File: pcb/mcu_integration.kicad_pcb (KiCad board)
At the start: 4 copper layers, 90.2 x 95.9 mm, 103 parts, among them IC1 TL7660IDGKR, IC10 AD844_OPAMP_MEL, IC3 FOD814_OPTO_NOSHD, IC5 FOD814_OPTO_MEL, IC6 AD844_OPAMP_AL, IC7 FOD814_OPTO_AL, IC8 AD844_OPAMP_NOSHD, IC9 TL081IDT, J5 DM3BT-DSF-PEJS, M1 MountingHole_Pad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

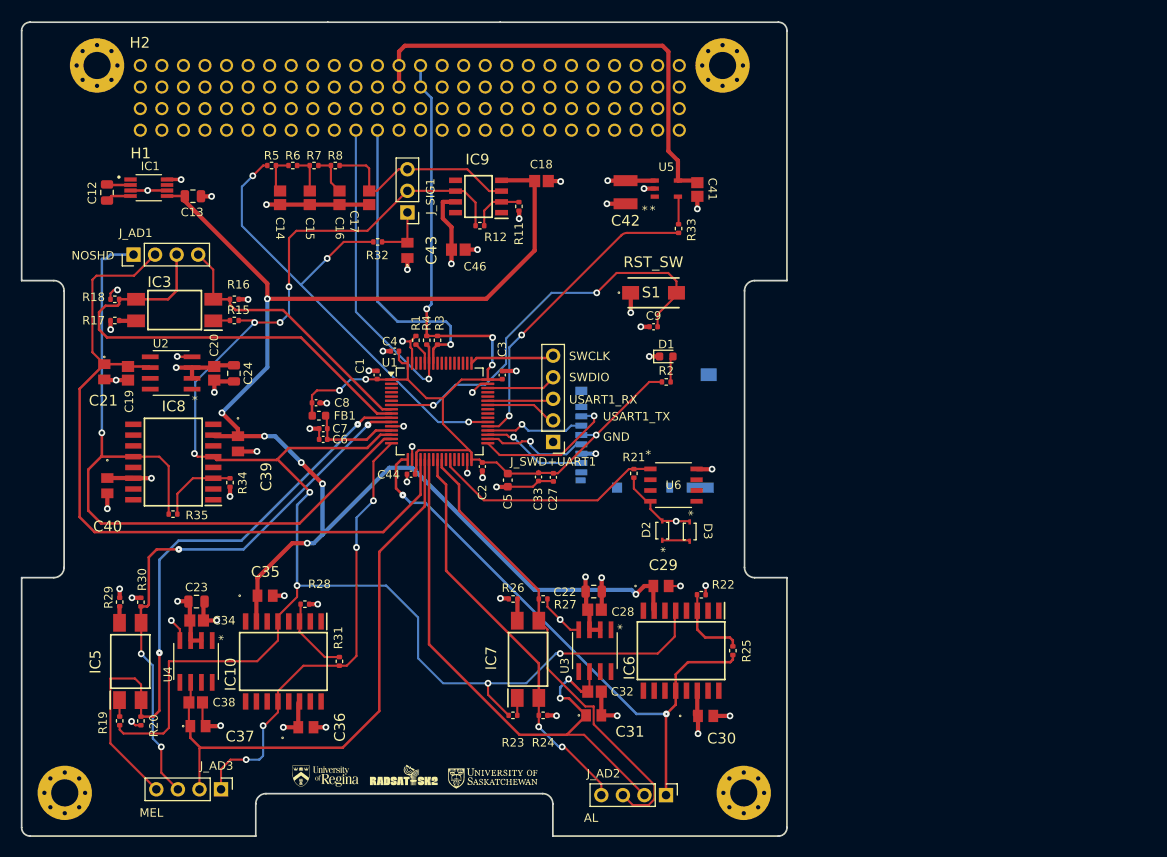
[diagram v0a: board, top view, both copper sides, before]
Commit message: Added copper pours to top and bottom layer, added 3.3v plane, spaced ICs to fit melanin caps, ungrounded connection pads, added stitching vias to outer edge
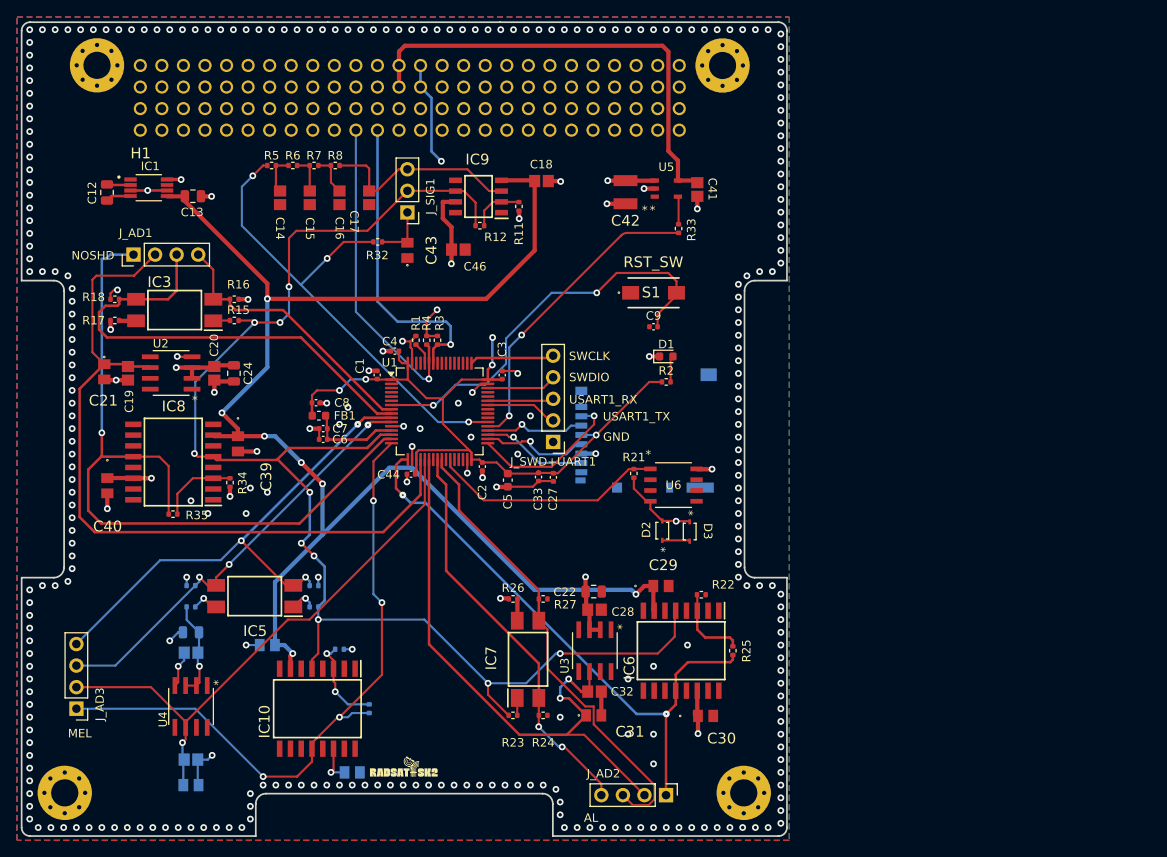
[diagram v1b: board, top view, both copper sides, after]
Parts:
- C23, C34, C35, C36, C37, C38, R19, R20, R28, R29, R30, R31: moved to B.Cu
- moved R19 26.5 mm to (127.0, 120.5), turned to 0 degrees
- moved R20 25.9 mm to (127.0, 118.0), turned to 0 degrees
- moved J_AD3 19.5 mm to (99.0, 132.5), turned to 180 degrees
- moved IC5 16.6 mm to (120.0, 119.2), turned to 180 degrees
- moved R29 8.42 mm to (112.5, 120.5), turned to 180 degrees
- moved C36 7.62 mm to (131.5, 140.0)
- moved C37 7.00 mm to (112.5, 141.5)
- moved IC10 6.86 mm to (127.4, 132.5)
- moved C38 6.76 mm to (112.5, 138.5)
- moved R28 6.70 mm to (130.0, 125.5)
- moved R31 6.59 mm to (133.5, 132.5)
- moved R30 6.21 mm to (112.5, 118.0), turned to 0 degrees
- moved C35 5.82 mm to (121.5, 125.0), turned to 180 degrees
- moved U4 5.34 mm to (112.5, 132.2)
- moved C34 3.84 mm to (112.5, 125.9), turned to 180 degrees
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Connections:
- M1 pad 1: GND -> unconnected-(M1-Pad1)
- M2 pad 1: GND -> unconnected-(M2-Pad1)
- M3 pad 1: GND -> unconnected-(M3-Pad1)
- M4 pad 1: GND -> unconnected-(M4-Pad1)
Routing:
- net GND: track 129.4 -> 90.8 mm, vias 51 -> 314
- net ADC1_IN0_SINE: track 201.3 -> 169.8 mm, vias 8 -> 10
- net ADC1_IN2_OPAMP_MEL: track 54.2 -> 77.8 mm
- net 3.3V Output: track 124.9 -> 101.8 mm, vias 6 -> 7
- net ADC1_IN12_OPTO_F_MEL: track 77.5 -> 59.5 mm, vias 2 -> 3
- net ADC1_IN13_OPTO_E_MEL: track 65.2 -> 50.7 mm, vias 4 -> 3
- net -5V Output: track 171.4 -> 176.2 mm
- net +5V: track 62.8 -> 65.2 mm, vias 13 -> 12
- net ADC1_IN5_VREF_MEL: track 68.0 -> 66.4 mm, vias 0 -> 1
- net Net-(IC10--IN): track 9.23 -> 10.7 mm, vias 0 -> 2
- net Net-(IC5-C): track 1.95 -> 3.29 mm, vias 0 -> 1
- net /SPI2_CS_NSS: track 16.9 -> 18.3 mm
- net Net-(IC5-AK): track 1.95 -> 3.06 mm, vias 0 -> 1
- added copper zone on In1.Cu, net 3.3V Output
- added copper zone on B.Cu, net GND
- added copper zone on F.Cu, net GND

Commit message: Conformed to JLC DFM
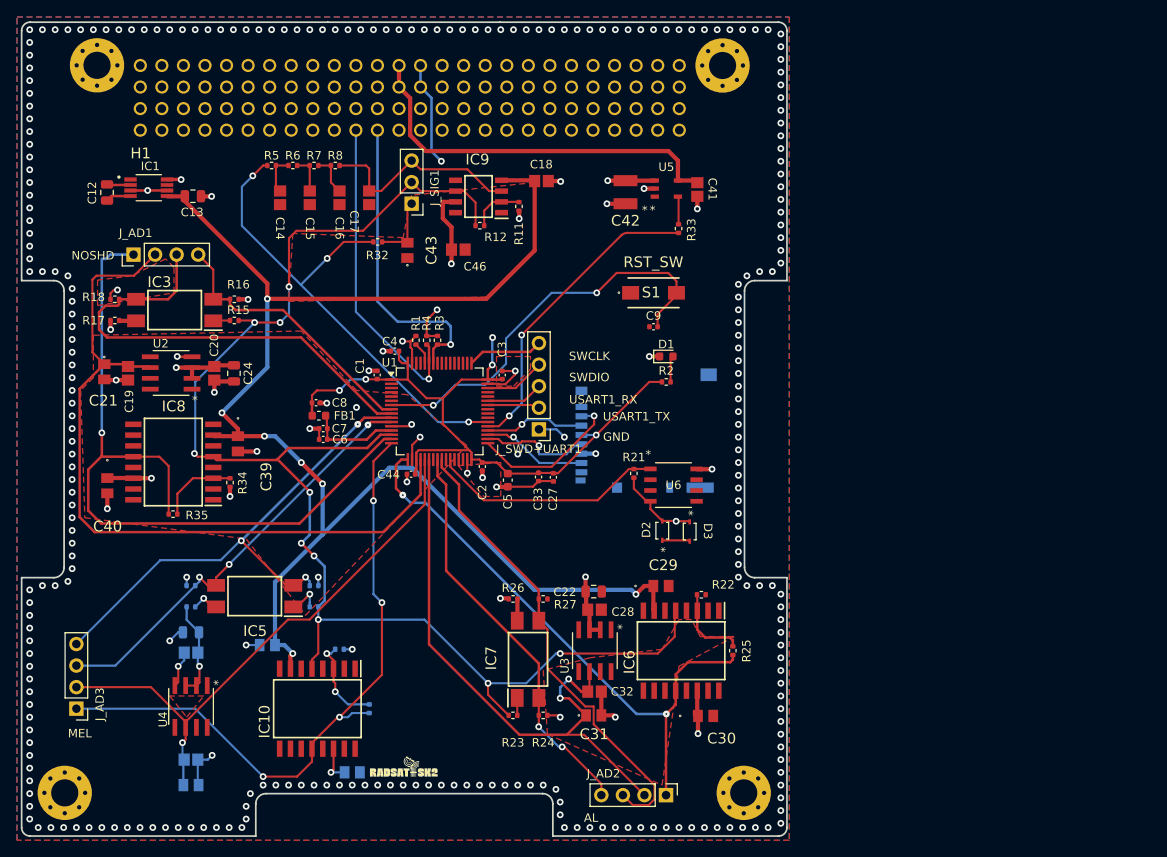
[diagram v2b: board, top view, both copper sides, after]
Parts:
- moved J_SWD+UART1 2.24 mm to (153.5, 99.6)
- moved J_SIG1 1.14 mm to (138.5, 73.0)
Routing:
- net GND: track 90.8 -> 101.4 mm, vias 314 -> 299
- net +5V_EXT: track 54.6 -> 46.3 mm
- net /USART1_TX: track 8.39 -> 6.16 mm
- net Net-(J_SIG1-Pin_1): track 6.61 -> 7.84 mm
- net Net-(IC5-AK): track 3.06 -> 4.07 mm
- net ADC1_IN0_SINE: track 169.8 -> 170.7 mm
- net RC_OUTPUT: track 24.0 -> 24.9 mm
- net /USART1_RX: track 7.55 -> 6.74 mm
- net /SWCLK: track 9.71 -> 8.93 mm
- net /SWDIO: track 7.94 -> 7.17 mm

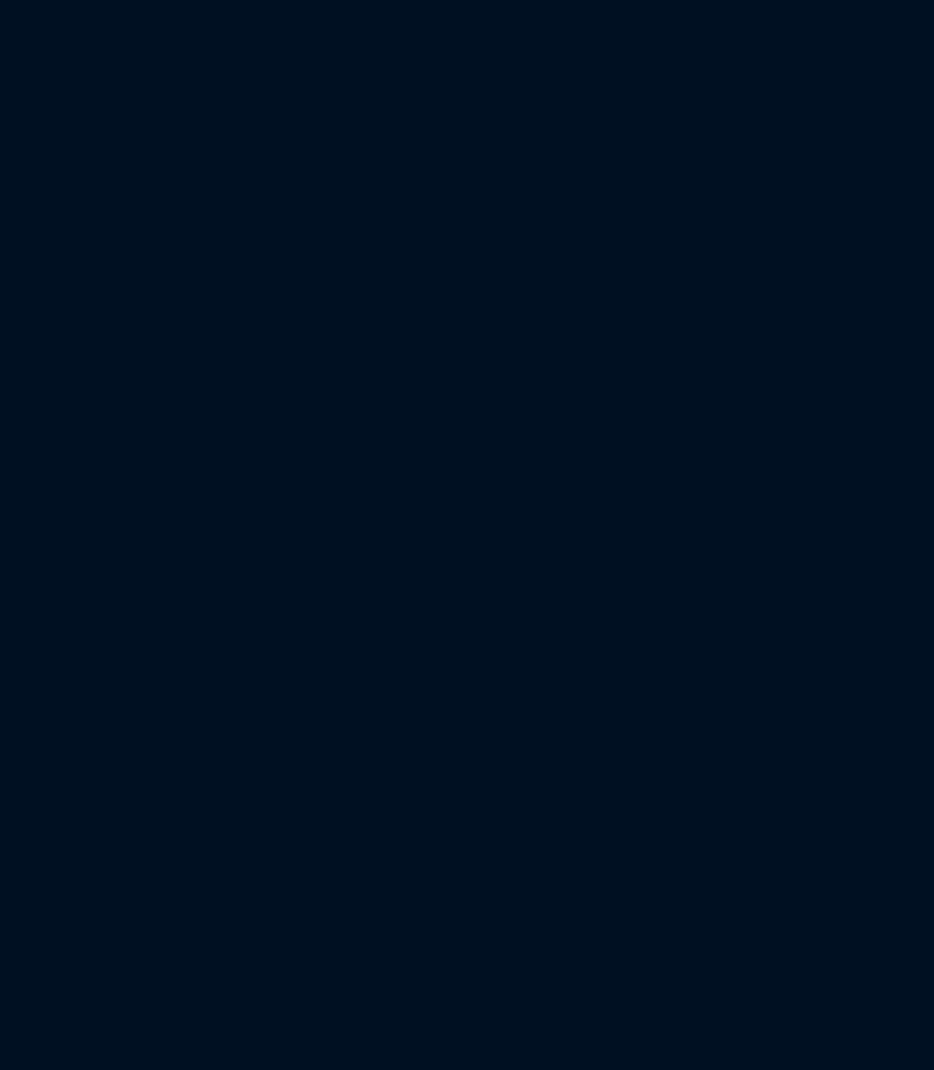
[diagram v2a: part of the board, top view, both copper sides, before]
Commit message: Added Shield Footprints
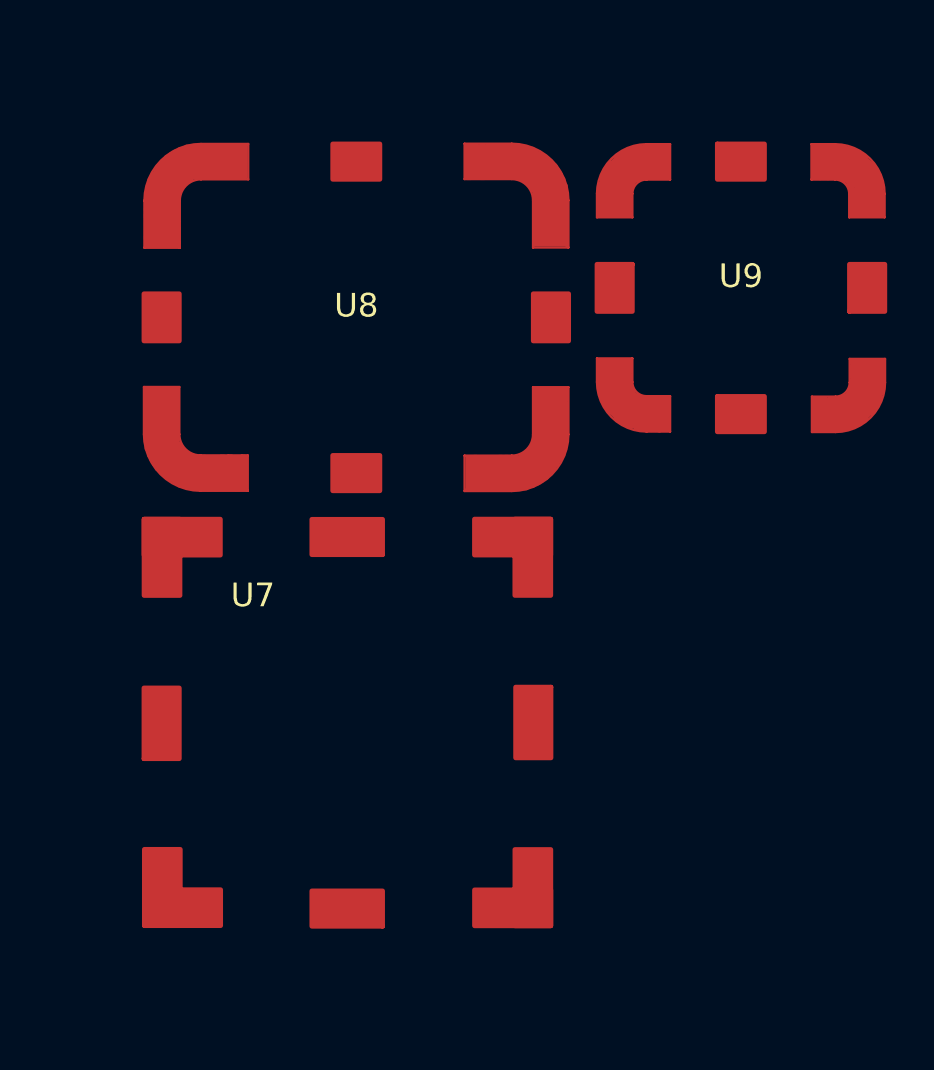
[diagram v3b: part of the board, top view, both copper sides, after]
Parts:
- added U7: ~, capstone:AD844 Shield, F.Cu at (202.6, 120.3)
- added U8: ~, capstone:FOD814 Shield, F.Cu at (202.9, 103.1)
- added U9: ~, capstone:REF192 Shield, F.Cu at (219.2, 101.8)

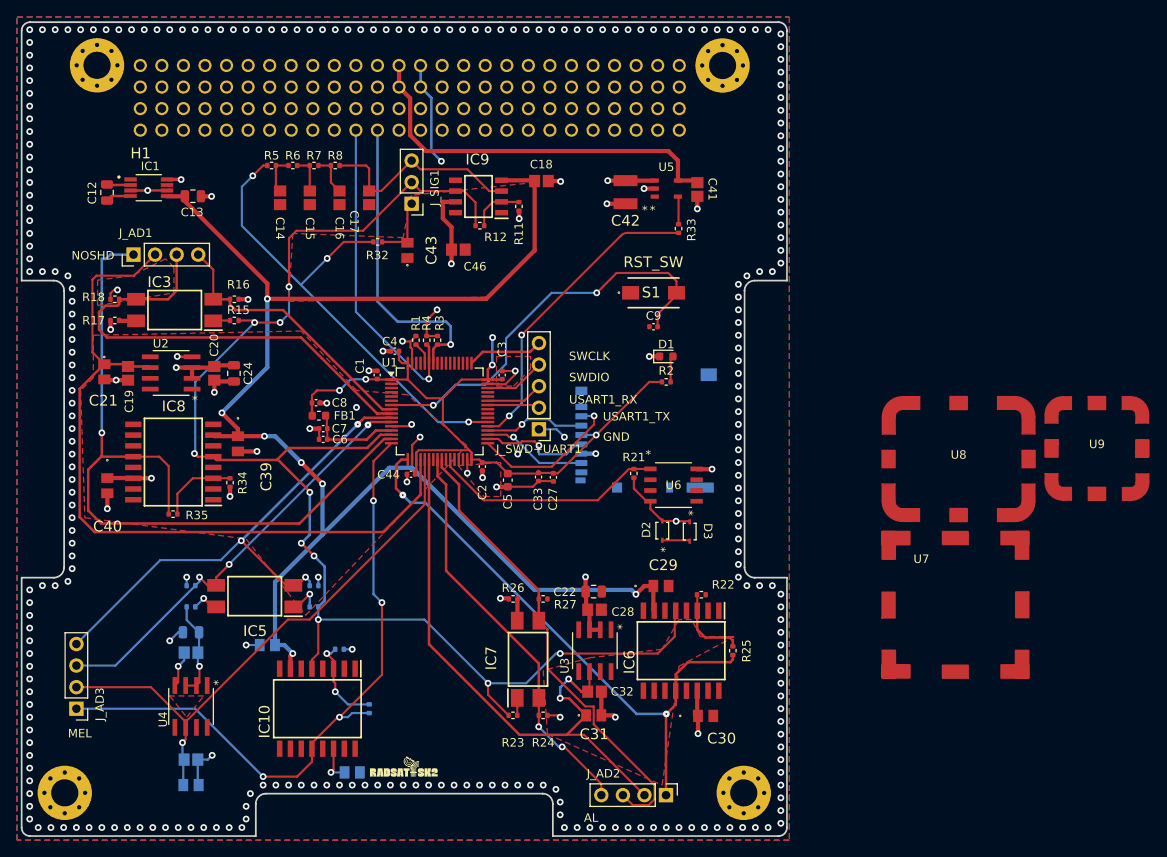
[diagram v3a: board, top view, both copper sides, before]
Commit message: Adjusted spacing of shields to allow for easier soldering
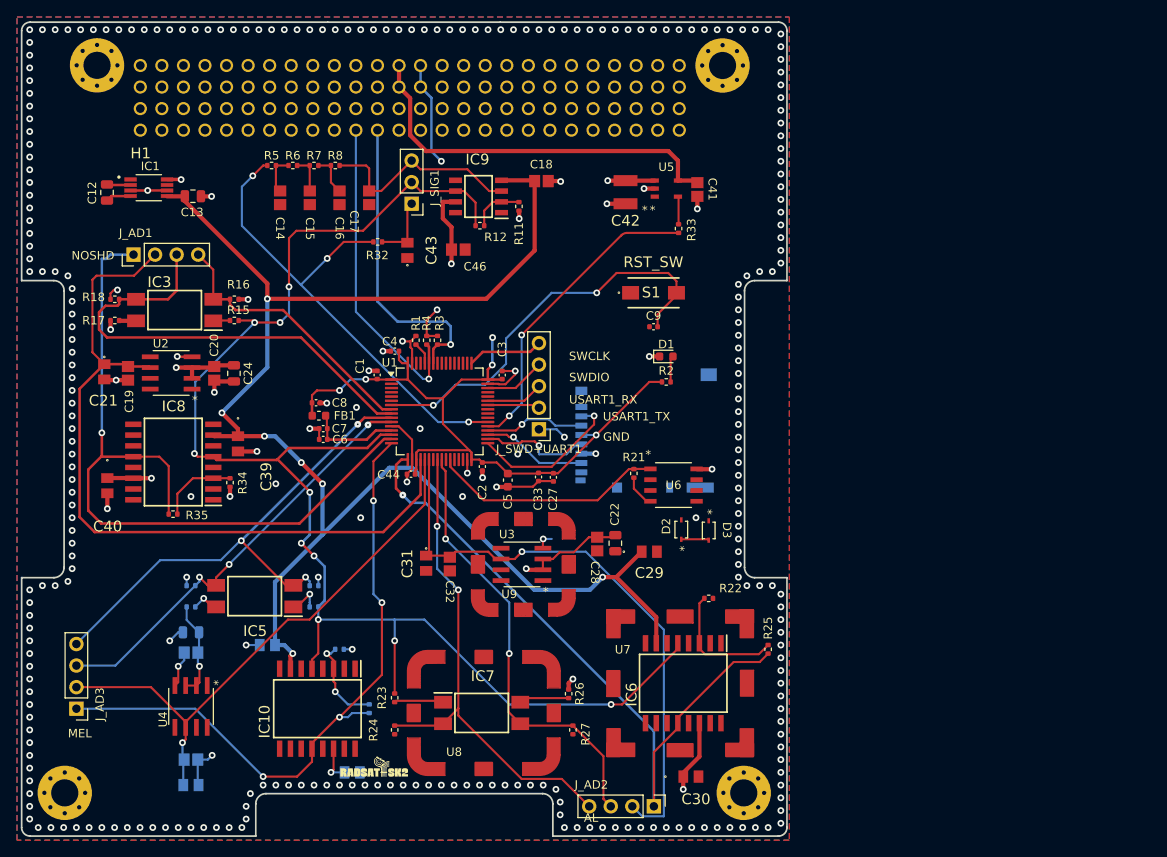
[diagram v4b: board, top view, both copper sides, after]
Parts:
- moved U9 68.9 mm to (151.7, 115.5), turned to -90 degrees
- moved U8 63.4 mm to (147.0, 133.0), turned to 180 degrees
- moved U7 33.7 mm to (170.1, 129.5)
- moved C31 26.7 mm to (140.2, 115.4), turned to -90 degrees
- moved C32 22.7 mm to (143.0, 115.5), turned to -90 degrees
- moved R24 17.6 mm to (136.5, 135.0), turned to -90 degrees
- moved R27 15.8 mm to (157.5, 135.0), turned to 90 degrees
- moved R23 14.1 mm to (136.5, 131.2), turned to 90 degrees
- moved U3 13.3 mm to (151.5, 115.5), turned to 180 degrees
- moved R26 12.9 mm to (157.0, 130.7), turned to 90 degrees
- moved IC7 8.35 mm to (146.8, 133.0), turned to 0 degrees
- moved C28 7.75 mm to (160.4, 113.1), turned to -90 degrees
- moved C30 7.36 mm to (171.4, 140.5)
- moved C22 6.24 mm to (162.5, 113.0), turned to -90 degrees
- moved C29 4.27 mm to (166.5, 114.0)
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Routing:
- net ADC1_IN14_OPTO_F_AL: track 47.9 -> 59.4 mm
- net ADC1_IN3_OPAMP_AL: track 70.6 -> 80.8 mm, vias 2 -> 1
- net GND: track 101.4 -> 92.6 mm, vias 299 -> 301
- net +5V: track 65.2 -> 72.7 mm
- net -5V Output: track 176.2 -> 182.9 mm
- net Net-(IC6--IN): track 9.50 -> 15.0 mm
- net Net-(IC7-C): track 2.57 -> 7.06 mm
- net Net-(IC7-AK): track 2.06 -> 6.30 mm
- net ADC1_IN0_SINE: track 170.7 -> 174.0 mm
- net ADC1_IN15_OPTO_E_AL: track 55.5 -> 52.7 mm, vias 0 -> 2
- net ADC1_IN6_VREF_AL: track 69.6 -> 70.5 mm, vias 2 -> 1
